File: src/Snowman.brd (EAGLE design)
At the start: 34.5 x 70.7 mm, 4 parts

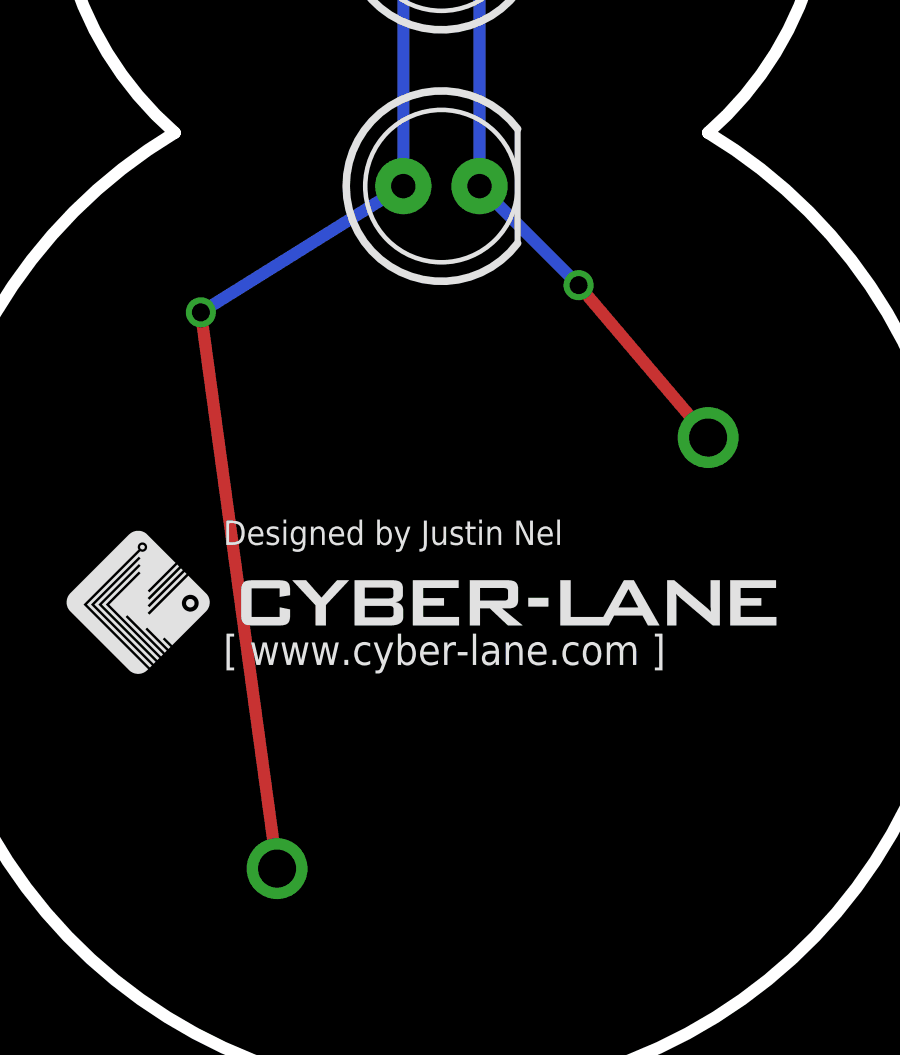
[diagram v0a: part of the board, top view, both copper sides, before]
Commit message: Corrected a small mistake on the ground planes
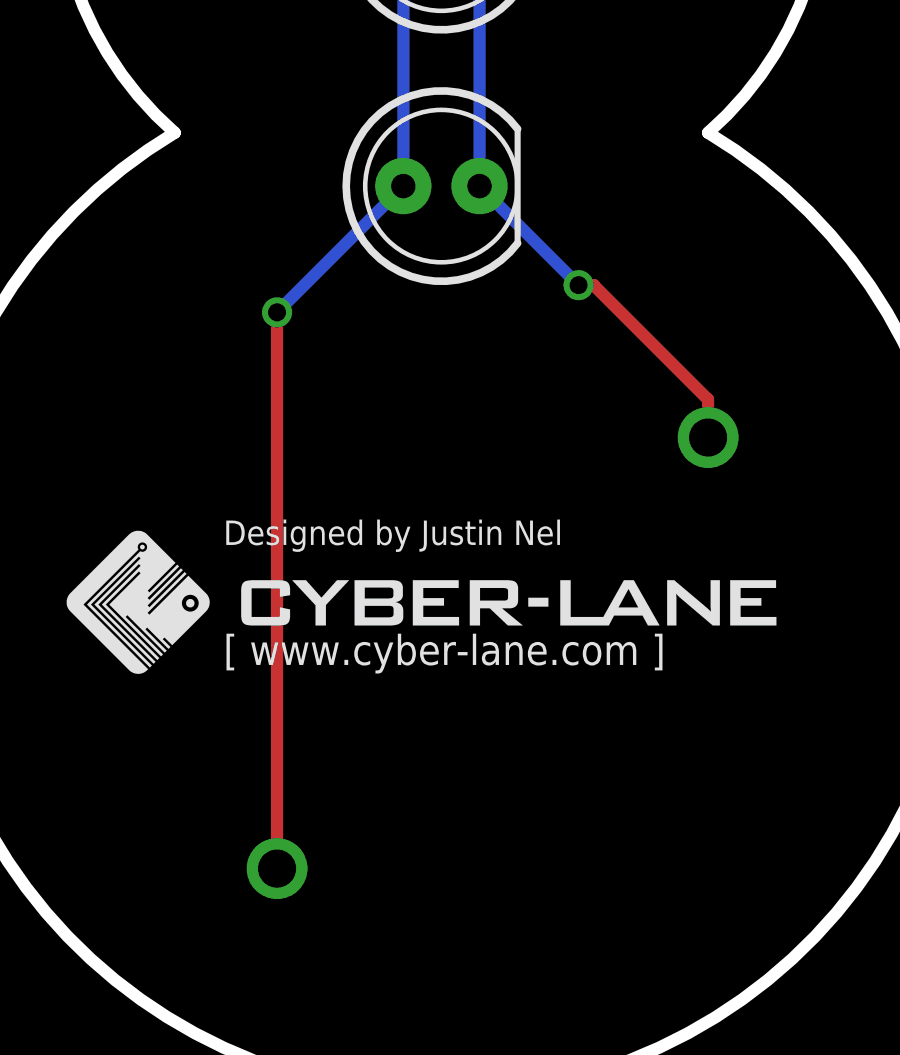
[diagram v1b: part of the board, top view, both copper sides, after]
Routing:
- net N$3: track 45.0 -> 42.8 mm
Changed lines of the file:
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@@
 <contactref element="LED1" pad="K"/>
 <contactref element="BATTERY_1" pad="+"/>
-<wire x1="26.67" y1="22.86" x2="22.352" y2="27.94" width="0.4064" layer="1"/>
+<wire x1="26.67" y1="22.86" x2="26.67" y2="24.13" width="0.4064" layer="1"/>
+<wire x1="26.67" y1="24.13" x2="22.86" y2="27.94" width="0.4064" layer="1"/>
+<wire x1="22.86" y1="27.94" x2="22.352" y2="27.94" width="0.4064" layer="1"/>
 <wire x1="22.352" y1="27.94" x2="19.05" y2="31.242" width="0.4064" layer="16"/>
 <wire x1="19.05" y1="31.242" x2="19.05" y2="39.624" width="0.4064" layer="16"/>
@@
 <contactref element="LED1" pad="A"/>
 <contactref element="BATTERY_1" pad="-"/>
-<wire x1="12.301590625" y1="8.4915875" x2="9.7615875" y2="27.0335875" width="0.4064" layer="1"/>
-<wire x1="9.7615875" y1="27.0335875" x2="16.51" y2="31.242" width="0.4064" layer="16"/>
+<wire x1="12.301590625" y1="8.4915875" x2="12.3015875" y2="27.0335875" width="0.4064" layer="1"/>
+<wire x1="12.3015875" y1="27.0335875" x2="16.51" y2="31.242" width="0.4064" layer="16"/>
 <wire x1="16.51" y1="31.242" x2="16.51" y2="39.624" width="0.4064" layer="16"/>
 <wire x1="16.51" y1="39.624" x2="16.51" y2="49.53" width="0.4064" layer="16"/>
-<via x="9.7615875" y="27.0335875" extent="1-16" drill="0.6"/>
+<via x="12.3015875" y="27.0335875" extent="1-16" drill="0.6"/>
 </signal>
 <signal name="GND">
-<polygon width="0.4064" layer="1">
+<polygon width="0.4064" layer="1" isolate="0.4064">
 <vertex x="0" y="0"/>
 <vertex x="36.83" y="0"/>
@@
 <vertex x="-1.27" y="0"/>
 </polygon>
-<polygon width="0.4064" layer="16">
+<polygon width="0.4064" layer="16" isolate="0.4064">
 <vertex x="-1.27" y="0"/>
 <vertex x="36.83" y="0"/>
